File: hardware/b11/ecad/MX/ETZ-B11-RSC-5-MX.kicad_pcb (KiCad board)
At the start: 2 copper layers, 131.5 x 85.8 mm, 44 parts, among them SW1 MX-Hotswap-1U, SW10 MX-Hotswap-1U, SW11 MX-Hotswap-1U, SW12 MX-Hotswap-1U, SW13 MX-Hotswap-1U, SW14 MX-Hotswap-1U, SW15 MX-Hotswap-1U, SW16 MX-Hotswap-1U, SW17 MX-Hotswap-1U, SW18 MX-Hotswap-1U, SW19 MX-Hotswap-1U, SW2 MX-Hotswap-1U, SW20 MX-Hotswap-1U, SW21 MX-Hotswap-1U, SW22 MX-Hotswap-1U, SW3 MX-Hotswap-1U, SW4 MX-Hotswap-1U, SW5 MX-Hotswap-1U, SW6 MX-Hotswap-1U, SW7 MX-Hotswap-1U, SW8 MX-Hotswap-1U, SW9 MX-Hotswap-1U

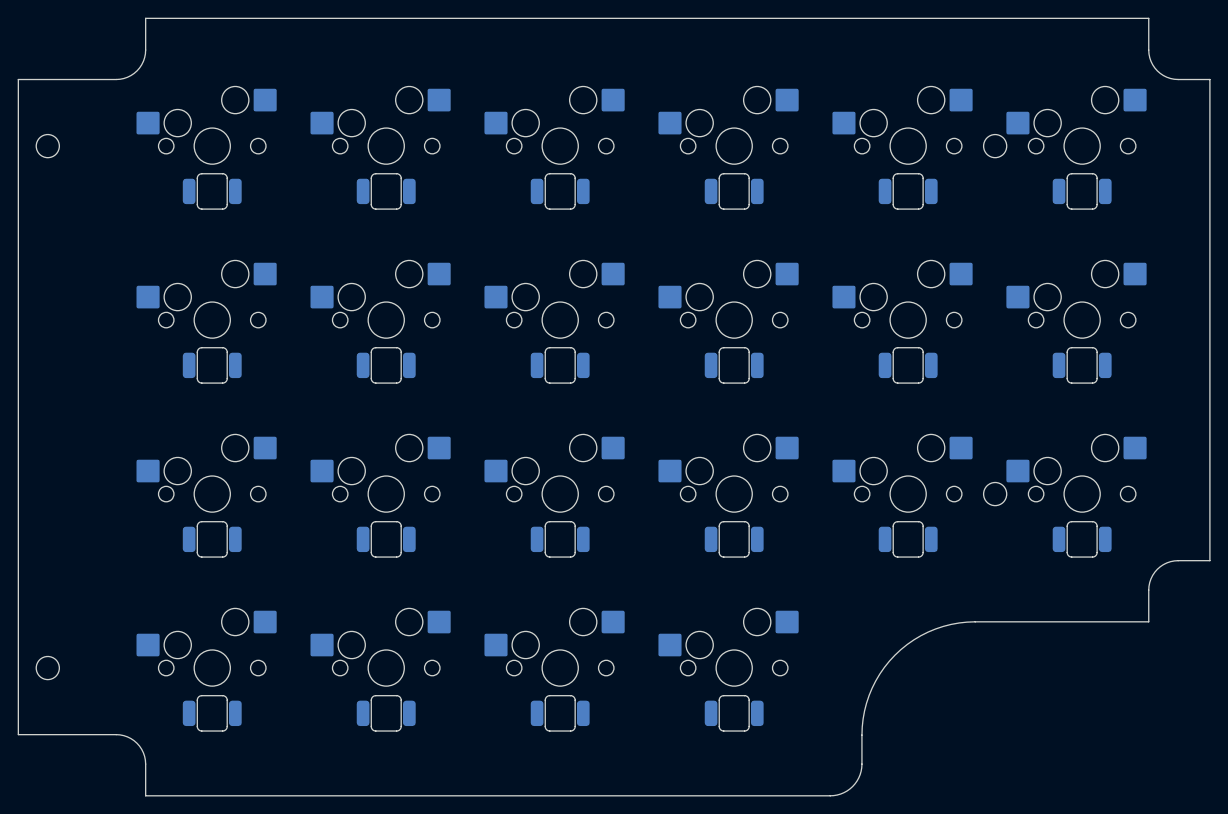
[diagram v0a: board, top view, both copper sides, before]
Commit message: refactor(hardware/b11): restructure ecad + tools, add KS-33 boards
- Rename PCB files: *-N → *-MX, *-L → *-CHOC-V2
- Reorganise ecad/ into per-family subfolders (MX/, CHOC-V2/, KS-33/)
- Add 8 blank KS-33 boards (outline only, human-populated ad-hoc)
- Apply JLCPCB-validated stackup (white/black/FR4 natural/black/white)
  to all 24 boards; SP boards at correct family thickness
- Add hardware/b11/tools/: config.py, placement.py, place-switch-sockets.py,
  place-switch-leds.py, place-display-leds.py — family-aware, non-destructive
- Archive old placement + generation scripts to hardware/scripts/_archive/
- Remove switch-origins.yaml (replaced by GRID_ORIGINS in config.py)
- Add PLAN.md tracking refactor progress

Co-Authored-By: Claude Sonnet 4.6 <noreply@anthropic.com>
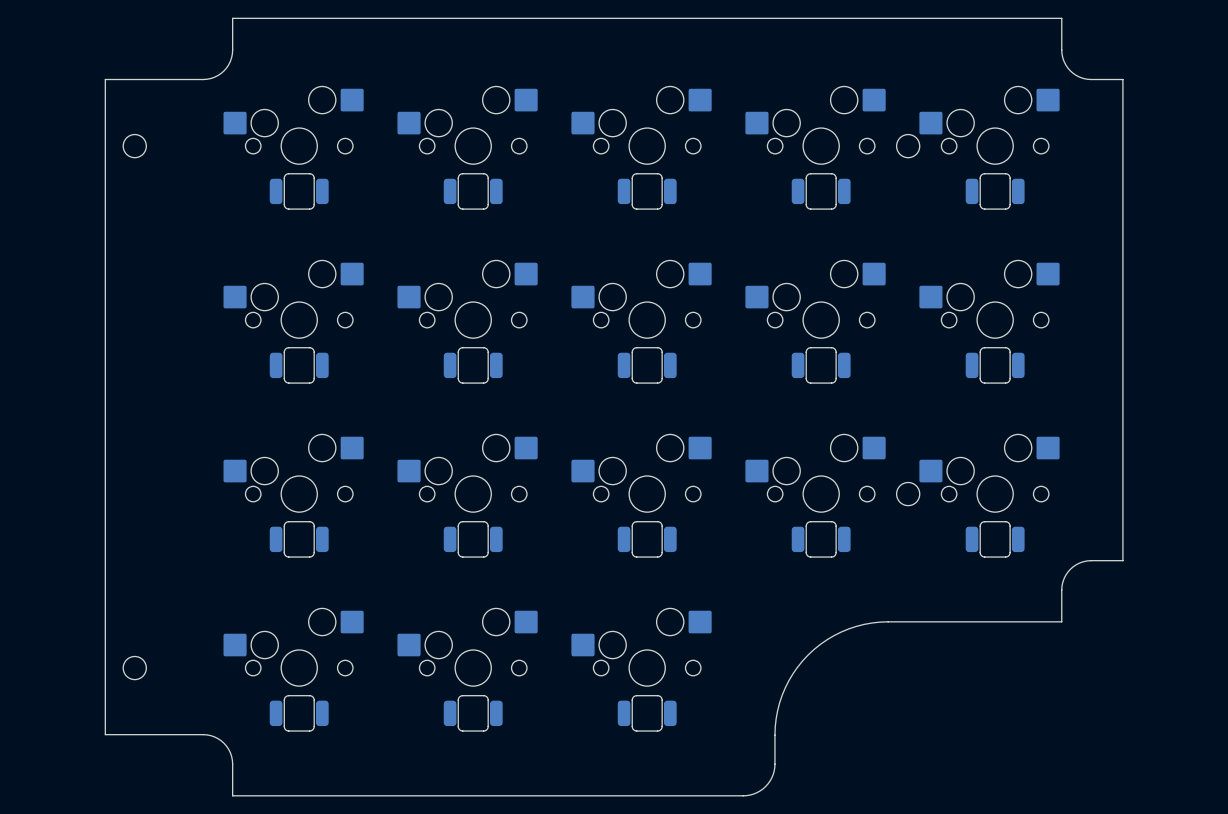
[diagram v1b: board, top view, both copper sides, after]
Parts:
- removed LED19, LED20, LED21, LED22: LED_SMD_6028_BackMount, LED_SMD_6028_BackMount
- removed SW19, SW20, SW21, SW22: MX-Hotswap-1U, MX-Hotswap-1U
- moved LED6 88.5 mm to (190.6, 97.5)
- moved SW6 88.5 mm to (190.6, 92.5)
- moved LED11 69.9 mm to (190.6, 116.7)
- moved SW11 69.9 mm to (190.6, 111.7)
- moved LED12 69.9 mm to (171.3, 116.7)
- moved SW12 69.9 mm to (171.3, 111.7)
- moved LED13 48.0 mm to (152.2, 116.7)
- moved LED14 48.0 mm to (132.9, 116.7)
- moved LED15 48.0 mm to (113.8, 116.7)
- moved SW13 48.0 mm to (152.2, 111.7)
- moved SW14 48.0 mm to (132.9, 111.7)
- moved SW15 48.0 mm to (113.8, 111.7)
- moved LED10 28.8 mm to (113.8, 97.5)
- moved LED7 28.8 mm to (171.3, 97.5)
- moved LED9 28.8 mm to (132.9, 97.5)
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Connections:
- SW10 pad 2: COL3 -> COL4
- SW11 pad 1: ROW1 -> ROW2
- SW11 pad 2: COL4 -> COL0
- SW12 pad 1: ROW1 -> ROW2
- SW12 pad 2: COL5 -> COL1
- SW13 pad 2: COL0 -> COL2
- SW14 pad 2: COL1 -> COL3
- SW15 pad 2: COL2 -> COL4
- SW16 pad 1: ROW2 -> ROW3
- SW16 pad 2: COL3 -> COL2
- SW17 pad 1: ROW2 -> ROW3
- SW17 pad 2: COL4 -> COL3
- SW18 pad 1: ROW2 -> ROW3
- SW18 pad 2: COL5 -> COL4
- SW6 pad 1: ROW0 -> ROW1
- SW6 pad 2: COL5 -> COL0
- SW7 pad 2: COL0 -> COL1
- SW8 pad 2: COL1 -> COL2
- SW9 pad 2: COL2 -> COL3
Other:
- board size 131.5 x 85.8 mm -> 112.3 x 85.8 mm
